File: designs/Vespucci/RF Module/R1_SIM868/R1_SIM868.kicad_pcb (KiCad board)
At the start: 4 copper layers, 42.6 x 30 mm, 56 parts, among them J1 U.FL IPEX, J2 U.FL IPEX, J3 SIM_Card, J4 PCIExpress, Q1 Q_NMOS_GDS, Q2 Q_NMOS_GDS, Q3 Q_NMOS_GDS, Q4 Q_NMOS_GDS, U1 SIM868, U2 RT9059, U3 TXS0108ERGY

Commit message: Initial D1, R1 Rev B
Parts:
- removed R10: 100K, Resistor_SMD:R_0402_1005Metric
- removed R11: 40K, Resistor_SMD:R_0402_1005Metric
- removed R9: 9k53, Resistor_SMD:R_0402_1005Metric
- added C17: 100nF, Capacitor_SMD:C_0402_1005Metric, F.Cu at (164.4, 106.0)
- added C18: 100nF, Capacitor_SMD:C_0402_1005Metric, F.Cu at (157.2, 110.7)
- added D10: D, Diode_SMD:D_SOD-123F, F.Cu at (158.4, 113.4)
- added D9: D, Diode_SMD:D_SOD-123F, F.Cu at (163.0, 113.4)
- added FB1: 250R, Inductor_SMD:L_0805_2012Metric, F.Cu at (153.6, 110.9)
- added L1: 2.2uH, Inductor_SMD:L_0603_1608Metric, F.Cu at (155.8, 110.2)
- C3, C6: moved to B.Cu
- R1, R2, R3, R7: value 51k -> 51K
- R12, R18, R8: value 9k53 -> 9K53
- U2: value RT9059 -> NCV891330; footprint Package_SO:SOIC-8-1EP_3.9x4.9mm_P1.27mm_EP2.41x3.3mm_ThermalVias -> Package_SO:SOIC-8-1EP_3.9x4.9mm_P1.27mm_EP2.29x3mm_ThermalVias
- moved C11 5.35 mm to (157.2, 108.7), turned to 90 degrees
- moved U2 4.08 mm to (161.6, 109.4)
- moved C3 2.04 mm to (164.4, 109.6)
- moved C6 0.86 mm to (162.1, 111.4), turned to 180 degrees
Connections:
- C11 pad 1: VDD -> Net-(C11-Pad1)
- C9 pad 1: VDD -> Net-(C11-Pad1)
- U2 pad 1: Net-(R10-Pad2) -> +BATT
- U2 pad 2: +BATT -> Net-(C17-Pad1)
- U2 pad 3: +BATT -> Net-(U2-Pad3)
- U2 pad 4: +BATT -> GND
- U2 pad 5: (no net) -> +BATT
- U2 pad 6: VDD -> Net-(C11-Pad1)
- U2 pad 8: GND -> Net-(C18-Pad1)
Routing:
- net VDD: track 44.3 -> 27.5 mm, vias 9 -> 8
- net +BATT: track 27.0 -> 40.1 mm, vias 2 -> 5
- net Net-(C17-Pad1): track 0.00 -> 13.0 mm
- net Net-(C18-Pad2): track 2.87 -> 14.9 mm
- net Net-(C11-Pad1): track 0.00 -> 10.00 mm
- net GND: track 70.6 -> 62.9 mm
- net Net-(C18-Pad1): track 0.00 -> 5.77 mm
- net Net-(R10-Pad2): track 2.69 -> 0.00 mm
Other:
- board text added: "R1 GSM/GNSS Radio Puccinelli Laboratories 20200519 REV B"
- board text removed: "R1 GSM/GNSS Radio Puccinelli Laboratories 20200308 REV A"

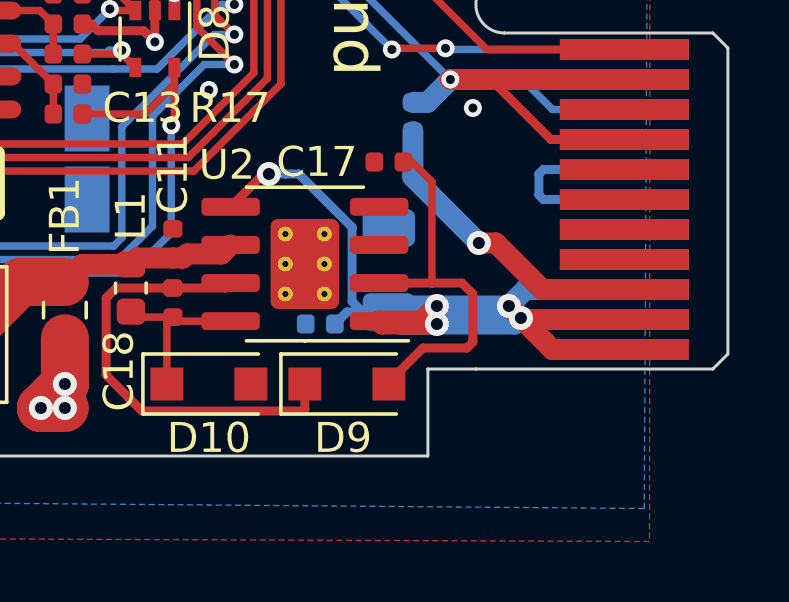
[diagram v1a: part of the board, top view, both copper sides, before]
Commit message: Corrected doubled symbol issue on R1
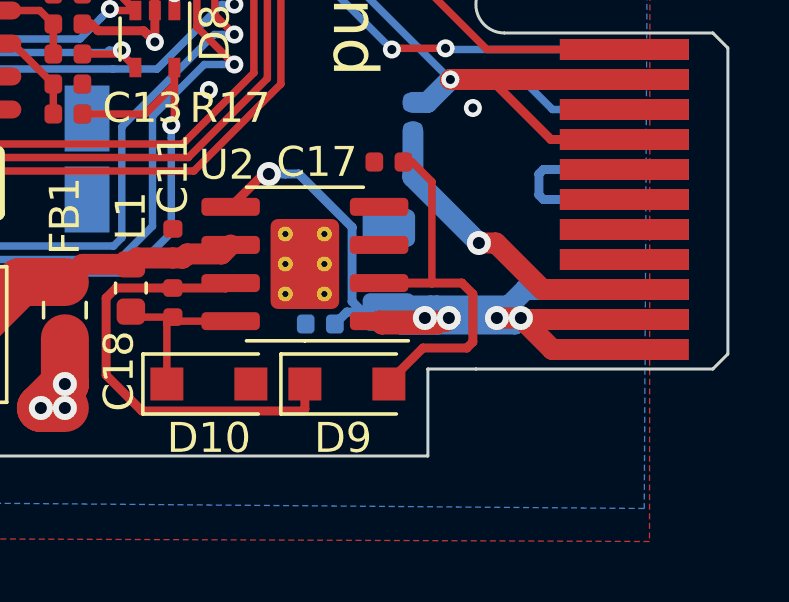
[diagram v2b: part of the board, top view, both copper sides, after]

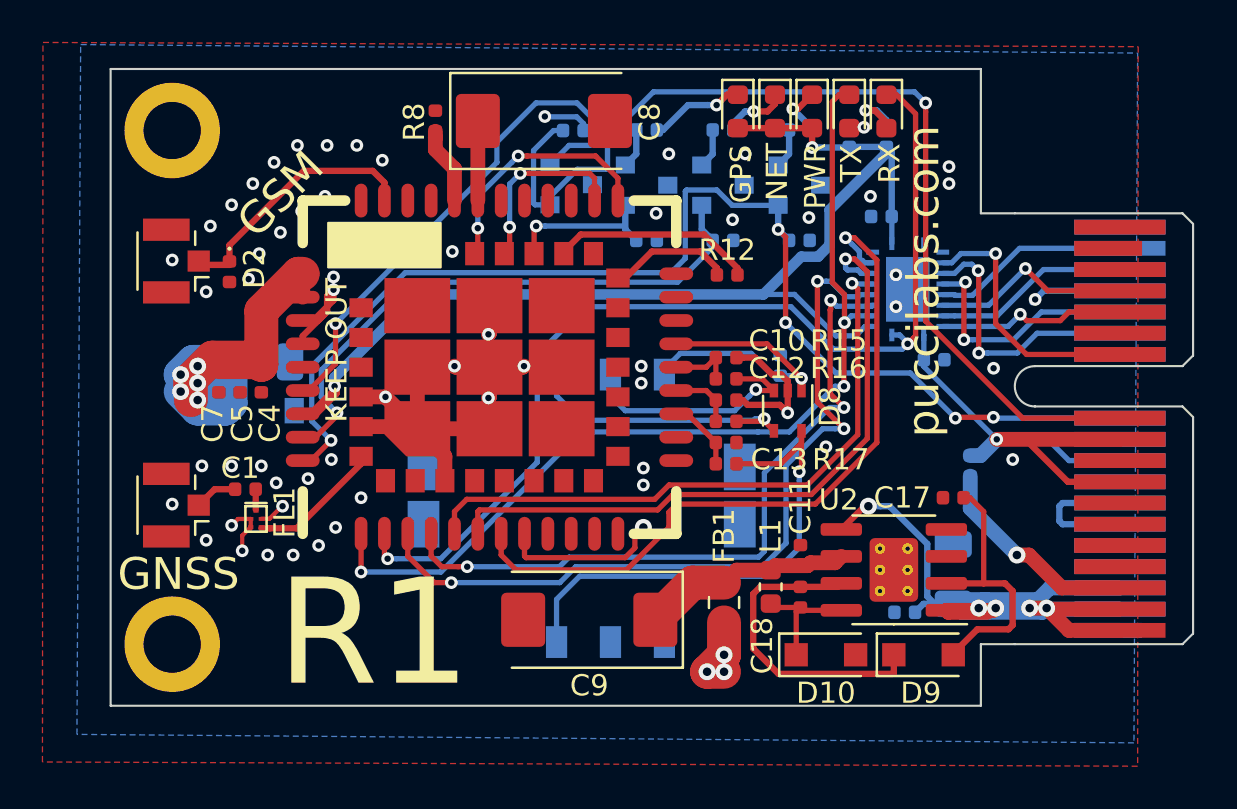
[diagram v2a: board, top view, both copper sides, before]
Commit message: R4R: P1 Rev B, R1 Rev B
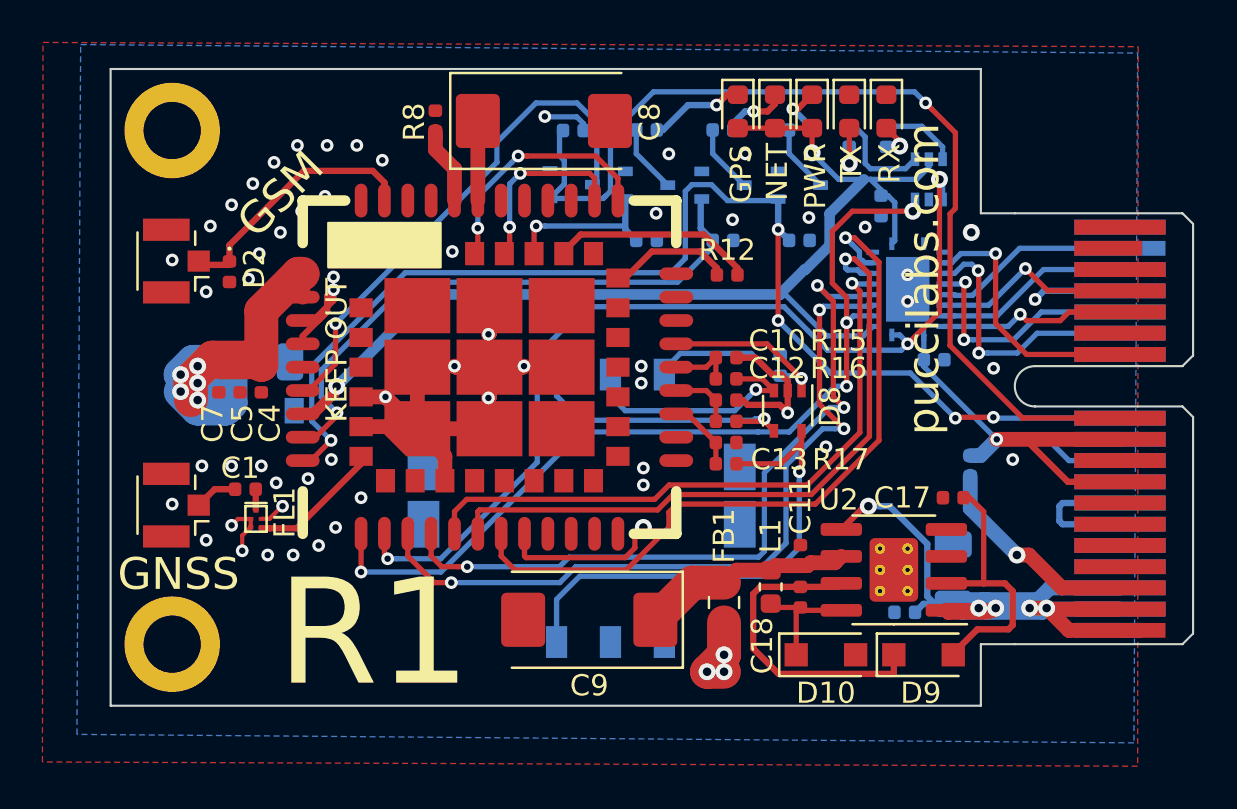
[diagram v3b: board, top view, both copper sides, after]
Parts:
- added G1: OSHW_logo, Custom_Footprints:OSHW_logo, B.Cu at (134.0, 113.0)
- added U4: NC7WZ14, Package_TO_SOT_SMD:SOT-363_SC-70-6, B.Cu at (163.2, 91.0)
- Q1, Q2, Q3, Q4: value Q_NMOS_GDS -> BSS138W; footprint Package_TO_SOT_SMD:SOT-23 -> Package_TO_SOT_SMD:SOT-323_SC-70
- moved C14 0.50 mm to (161.0, 92.2), turned to 270 degrees
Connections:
- C14 pad 1: /VDD_EXT -> VCC
- D1 pad 2: /VDD_EXT -> VCC
- D3 pad 2: /VDD_EXT -> VCC
- D4 pad 2: /VDD_EXT -> VCC
- D6 pad 1: /dTX -> GND
- D7 pad 1: /dRX -> GND
- Q1 pad 2: Net-(Q1-Pad2) -> GND
- Q1 pad 3: GND -> Net-(Q1-Pad3)
- Q2 pad 2: Net-(Q2-Pad2) -> GND
- Q2 pad 3: GND -> Net-(Q2-Pad3)
- Q3 pad 2: Net-(Q3-Pad2) -> GND
- Q3 pad 3: GND -> Net-(Q3-Pad3)
- Q4 pad 2: Net-(Q4-Pad2) -> GND
- Q4 pad 3: GND -> Net-(Q4-Pad3)
- R13 pad 1: /VDD_EXT -> Net-(D6-Pad2)
- R13 pad 2: Net-(D6-Pad2) -> Net-(R13-Pad2)
- R14 pad 1: /VDD_EXT -> Net-(D7-Pad2)
- R14 pad 2: Net-(D7-Pad2) -> Net-(R14-Pad2)
- R4 pad 1: Net-(Q1-Pad2) -> Net-(Q1-Pad3)
- R5 pad 1: Net-(Q2-Pad2) -> Net-(Q2-Pad3)
- R6 pad 1: Net-(Q3-Pad2) -> Net-(Q3-Pad3)
- U1 pad 39: Net-(Q4-Pad2) -> Net-(Q4-Pad3)
- U1 pad 40: /VDD_EXT -> VCC
- U3 pad 10: /VDD_EXT -> VCC
- U3 pad 2: /VDD_EXT -> VCC
- U3 pad 4: /dCTS -> /dRTS
- U3 pad 5: /dRTS -> /dCTS
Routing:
- net /VDD_EXT: track 53.0 -> 0.00 mm, vias 2 -> 0
- net VCC: track 0.00 -> 52.5 mm, vias 0 -> 2
- net Net-(Q4-Pad2): track 25.0 -> 0.00 mm, vias 1 -> 0
- net Net-(Q4-Pad3): track 0.00 -> 24.5 mm, vias 0 -> 1
- net Net-(R13-Pad2): track 0.00 -> 4.85 mm
- net Net-(R14-Pad2): track 0.00 -> 3.63 mm
- net /dRX: track 48.2 -> 44.9 mm, vias 2 -> 3
- net Net-(Q3-Pad3): track 0.00 -> 3.22 mm
- net Net-(Q2-Pad3): track 0.00 -> 3.22 mm
- net Net-(Q1-Pad3): track 0.00 -> 3.22 mm
- net /dTX: track 44.2 -> 42.0 mm, vias 3 -> 4
- net Net-(Q1-Pad2): track 1.86 -> 0.00 mm
- net Net-(Q3-Pad2): track 1.86 -> 0.00 mm
- net Net-(Q2-Pad2): track 1.86 -> 0.00 mm
- net /dRTS: track 37.7 -> 35.9 mm
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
